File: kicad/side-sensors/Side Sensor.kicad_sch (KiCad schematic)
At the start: 0 parts

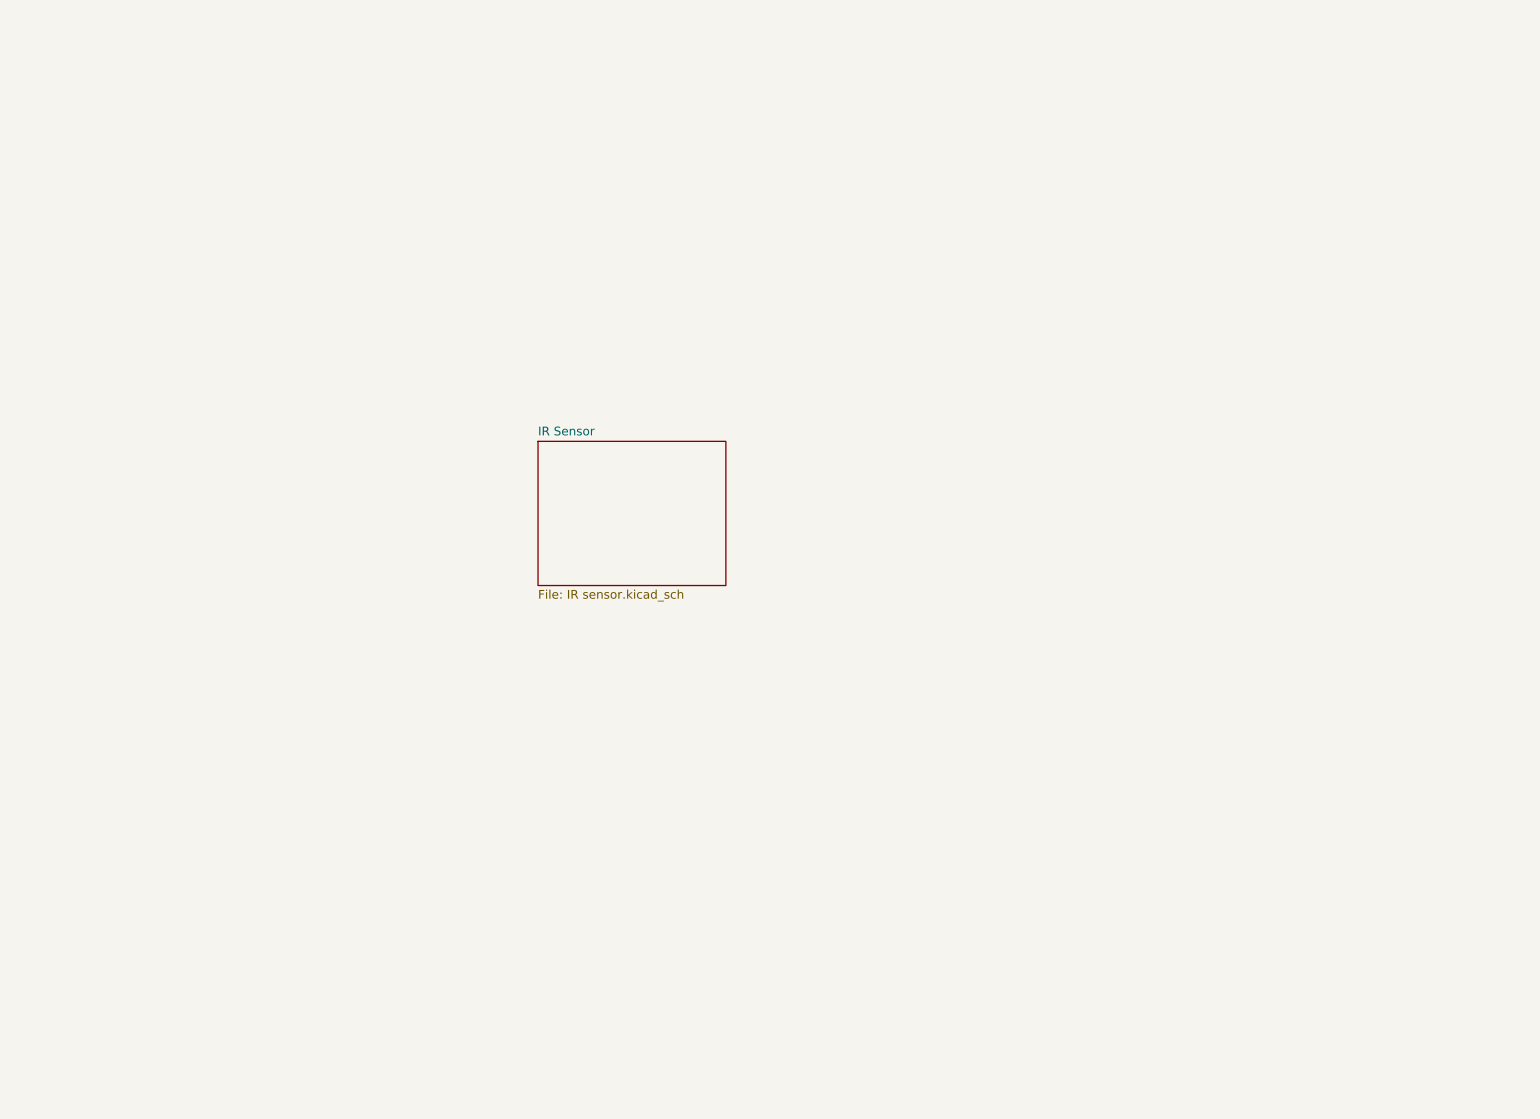
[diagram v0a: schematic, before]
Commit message: Side sensor board rev 2 (VL53L0X + IRM-H638T, JST SH); mounting holes on dock and sensor boards
- kicad/side-sensors: VL53L0X (C91199) replaces the NRND VL6180 and its 2.8 V LDO;
  top-looking IRM-H638T replaces the TSOP38238; ZX-SH1.0-7PWT connector, same pinout;
  10k XSHUT/GPIO1 pull-ups, no local I2C pull-ups; refs 84xx; libs from ../main
- main-phone SIDE-R1: ZX-ZH1.5-7PWT -> ZX-SH1.0-7PWT
- mounting holes: dock 4x M3 (H8201-H8204), ToF board 2x M2 (H8301/H8302),
  side board 2x M2 (H8401/H8402)
- JLCImport: VL53L0CXV0DH_1 symbol, footprint, 3D model
- docs: side board README, SPEC, READMEs; IRM-H638T pinout confirmed

Co-Authored-By: Claude Opus 5.5 (1M context) <noreply@anthropic.com>
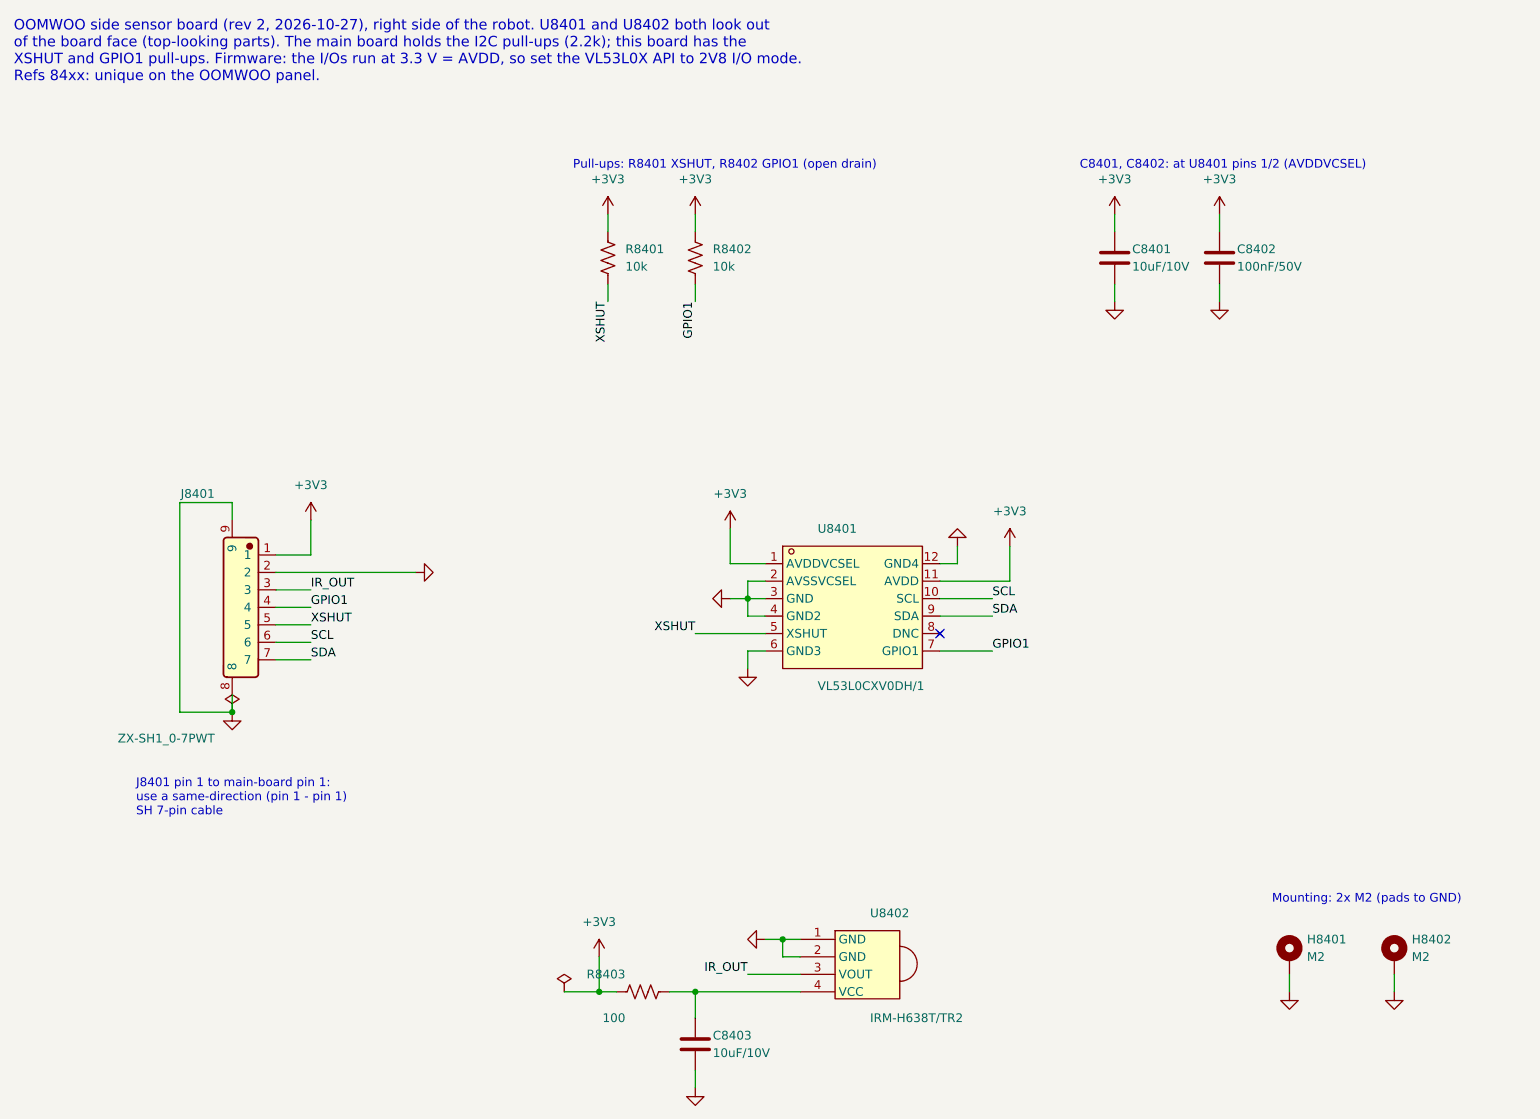
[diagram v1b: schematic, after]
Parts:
- added C8401, C8403: 10uF/10V, Capacitor_SMD:C_0603_1608Metric, symbol Device:C
- added C8402: 100nF/50V, Capacitor_SMD:C_0603_1608Metric, symbol Device:C
- added H8401, H8402: M2, MountingHole:MountingHole_2.2mm_M2_Pad, symbol Mechanical:MountingHole_Pad
- added J8401: ZX-SH1_0-7PWT, JLCImport:ZX-SH1_0-7PWT, symbol JLCImport:ZX-SH1_0-7PWT
- added R8401, R8402: 10k, Resistor_SMD:R_0603_1608Metric, symbol Device:R_US
- added R8403: 100, Resistor_SMD:R_0603_1608Metric, symbol Device:R_US
- added U8401: VL53L0CXV0DH/1, JLCImport:VL53L0CXV0DH_1, symbol JLCImport:VL53L0CXV0DH_1
- added U8402: IRM-H638T/TR2, JLCImport:IRM-H638T, symbol JLCImport:IRM-H638T
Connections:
- new net: C8403.1, R8403.2, U8402.4 (VCC)
- new net +3V3: C8401.1, C8402.1, J8401.1, R8401.1, R8402.1, R8403.1, U8401.1 (AVDDVCSEL), U8401.11 (AVDD)
- new net GND: C8401.2, C8402.2, C8403.2, H8401.1, H8402.1, J8401.2, J8401.8, J8401.9, U8401.12 (GND4), U8401.2 (AVSSVCSEL), U8401.3 (GND), U8401.4 (GND2), U8401.6 (GND3), U8402.1 (GND), U8402.2 (GND)
- new net GPIO1: J8401.4, R8402.2, U8401.7 (GPIO1)
- new net IR_OUT: J8401.3, U8402.3 (VOUT)
- new net SCL: J8401.6, U8401.10 (SCL)
- new net SDA: J8401.7, U8401.9 (SDA)
- new net XSHUT: J8401.5, R8401.2, U8401.5 (XSHUT)
- no-connect marks 0 -> 1
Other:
- removed sheet IR Sensor
- note added: "C8401, C8402: at U8401 pins 1/2 (AVDDVCSEL)"
- note added: "J8401 pin 1 to main-board pin 1: use a same-direction (pin 1 - pin 1) SH 7-pin cable"
- note added: "Mounting: 2x M2 (pads to GND)"
- note added: "OOMWOO side sensor board (rev 2, 2026-10-27), right side of the robot. U8401 and U8402 both look out of the board face (top-looking parts). The main board holds the I2C pull-ups (2.2k); this board has the XSHUT and GPIO1 pull-ups. Firmware: the I/Os run at 3.3 V = AVDD, so set the VL53L0X API to 2V8 I/O mode. Refs 84xx: unique on the OOMWOO panel."
- note added: "Pull-ups: R8401 XSHUT, R8402 GPIO1 (open drain)"
- company: (none) -> OOMWOO side sensor
- title: (none) -> Side sensor board (right side)

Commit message: Per-board reference ranges, J1 spare header, IMU AD0 pull-down, BOM outputs
- reference ranges: main-phone 1-999, dock 1000s, front ToF 2000s, side 3000s,
  cliff 4000s, rear IR 5000s, Hall 6000s (main-phone 7xxx parts renumbered
  below 1000; sensor boards and dock moved from 8xxx)
- main-phone: J7301 -> J1, a fitted 2x7 0.1" header with spares only
  (3.3 V, 5 V, I2C4, UART PC10/PC11, PA8-PA10, PD4, PE2, PE6, GND)
- IMU: AP_AD0 pulled low by R217 (address 0x68); INT2 on test pad TP1;
  FSYNC reachable on R211; R18/R72 removed
- tools/export.py replaces export_pdfs.py: schematic PDF and JLC-style BOM in
  each board's output/ folder; --pcb adds Gerbers, placement and STEP
- cliff and rear IR projects: fix top-level sheet left over from a copy
- Hall board: visual tidy-up

Co-Authored-By: Claude Opus 5.5 <noreply@anthropic.com>
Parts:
- renumbered C8401 to C3001, C8402 to C3002, C8403 to C3003, H8401 to H3001, H8402 to H3002, J8401 to J3001, R8401 to R3001, R8402 to R3002, R8403 to R3003, U8401 to U3001, U8402 to U3002
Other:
- note added: "C3001, C3002: at U3001 pins 1/2 (AVDDVCSEL)"
- note added: "J3001 pin 1 to main-board pin 1: use a same-direction (pin 1 - pin 1) SH 7-pin cable"
- note added: "OOMWOO side sensor board (rev 2, 2026-10-27), right side of the robot. U3001 and U3002 both look out of the board face (top-looking parts). The main board holds the I2C pull-ups (2.2k); this board has the XSHUT and GPIO1 pull-ups. Firmware: the I/Os run at 3.3 V = AVDD, so set the VL53L0X API to 2V8 I/O mode. Refs in the 3000s: each board has its own range."
- note added: "Pull-ups: R3001 XSHUT, R3002 GPIO1 (open drain)"
- note removed: "C8401, C8402: at U8401 pins 1/2 (AVDDVCSEL)"
- note removed: "J8401 pin 1 to main-board pin 1: use a same-direction (pin 1 - pin 1) SH 7-pin cable"
- note removed: "OOMWOO side sensor board (rev 2, 2026-10-27), right side of the robot. U8401 and U8402 both look out of the board face (top-looking parts). The main board holds the I2C pull-ups (2.2k); this board has the XSHUT and GPIO1 pull-ups. Firmware: the I/Os run at 3.3 V = AVDD, so set the VL53L0X API to 2V8 I/O mode. Refs 84xx: unique on the OOMWOO panel."
- note removed: "Pull-ups: R8401 XSHUT, R8402 GPIO1 (open drain)"
